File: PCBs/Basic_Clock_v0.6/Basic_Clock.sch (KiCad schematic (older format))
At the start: 37 parts, among them J1 Conn_01x04_Female, J3 Screw_Terminal_01x02, J4 Screw_Terminal_01x02, J5 Conn_01x03_Female, SW2 SW_Push, SW3 SW_Push, SW4 SW_Push, U1 LM317_TO-220, U2 ATmega328P-PU, U3 MAX485E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

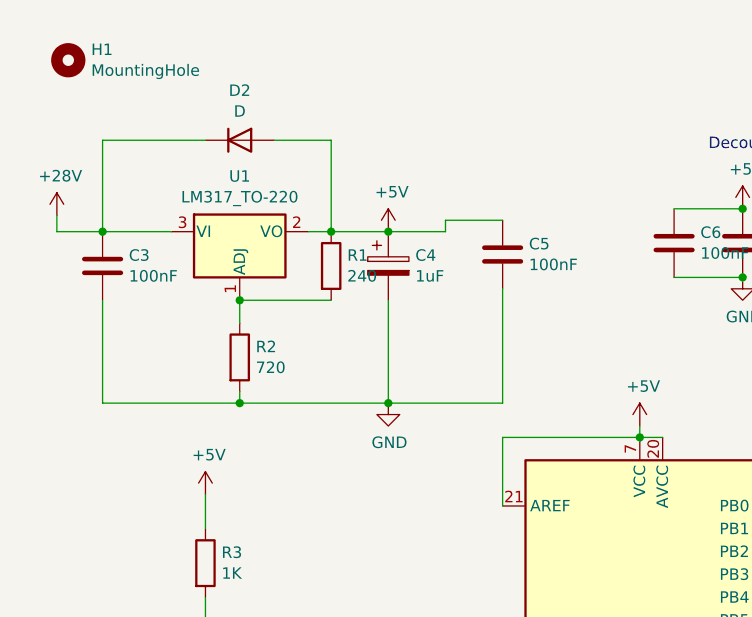
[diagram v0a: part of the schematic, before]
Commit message: Fixed ICSP Pinout
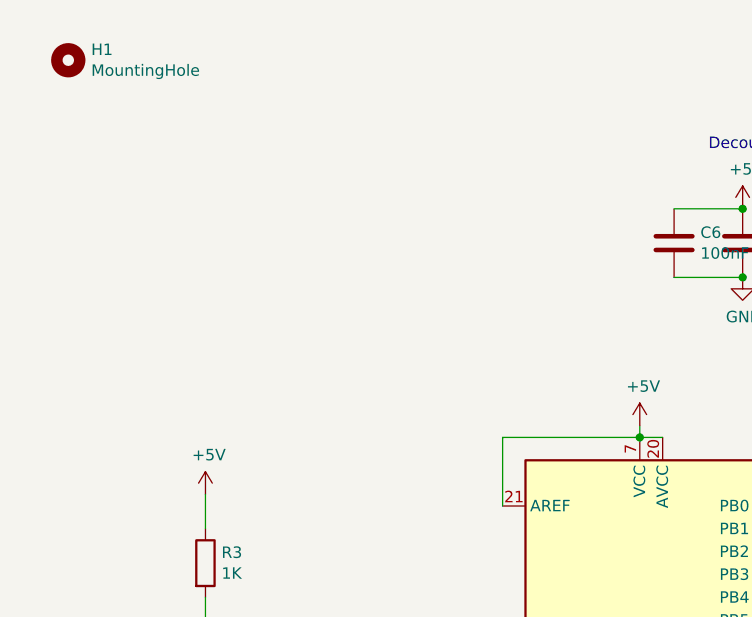
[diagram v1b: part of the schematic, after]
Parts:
- removed C3, C5: 100nF, Capacitor_THT:C_Rect_L7.0mm_W3.5mm_P5.00mm, symbol Device:C
- removed C4: 1uF, Capacitor THT:CP_Radial_D5.0mm_P2.00mm, symbol Device:CP
- removed D2: D, Diode THT:D_T-1_P10.16mm_Horizontal, symbol Device:D
- removed R1: 240, Resistor:R_Axial_DIN0309_L9.0mm_D3.2mm_P12.70mm_Horizontal, symbol Device:R
- removed R2: 720, Resistor:R_Axial_DIN0309_L9.0mm_D3.2mm_P12.70mm_Horizontal, symbol Device:R
- removed U1: LM317_TO-220, TO SOT THT:TO-220-3_Vertical, symbol Regulator_Linear:LM317_TO-220
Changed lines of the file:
@@
 	3350 5550 3350 5300
-$Comp
-L Regulator_Linear:LM317_TO-220 U1
-U 1 1 5F5E354F
-P 1600 1400
-F 0 "U1" H 1600 1642 50  0000 C CNN
-F 1 "LM317_TO-220" H 1600 1551 50  0000 C CNN
-F 2 "TO SOT THT:TO-220-3_Vertical" H 1600 1650 50  0001 C CIN
-F 3 "https://www.distrelec.ch/Web/Downloads/a_/en/tnSTM-LM317_data_en.pdf" H 1600 1400 50  0001 C CNN
-	1    1600 1400
-	1    0    0    -1
-$EndComp
 $Comp
 L Device:Crystal Y1
@@
 	1    0    0    -1
 $EndComp
-$Comp
-L Device:C C3
-U 1 1 5F5EFD99
-P 1000 1550
-F 0 "C3" H 1115 1596 50  0000 L CNN
-F 1 "100nF" H 1115 1505 50  0000 L CNN
-F 2 "Capacitor_THT:C_Rect_L7.0mm_W3.5mm_P5.00mm" H 1038 1400 50  0001 C CNN
-F 3 "https://www.distrelec.ch/en/ceramic-capacitor-100nf-50v-10-kemet-c322c104k5r5ta7301/p/16571681" H 1000 1550 50  0001 C CNN
-	1    1000 1550
-	1    0    0    -1
-$EndComp
-$Comp
-L Device:R R1
-U 1 1 5F5F0629
-P 2000 1550
-F 0 "R1" H 2070 1596 50  0000 L CNN
-F 1 "240" H 2070 1505 50  0000 L CNN
-F 2 "Resistor:R_Axial_DIN0309_L9.0mm_D3.2mm_P12.70mm_Horizontal" V 1930 1550 50  0001 C CNN
-F 3 "https://www.distrelec.ch/de/widerstand-600mw-240ohm-vishay-mbb02070c2400fct00/p/16059199?q=240ohm&pos=1&origPos=1&origPageSize=10&track=true" H 2000 1550 50  0001 C CNN
-	1    2000 1550
-	1    0    0    -1
-$EndComp
-$Comp
-L Device:R R2
-U 1 1 5F5F10C3
-P 1600 1950
-F 0 "R2" H 1670 1996 50  0000 L CNN
-F 1 "720" H 1670 1905 50  0000 L CNN
-F 2 "Resistor:R_Axial_DIN0309_L9.0mm_D3.2mm_P12.70mm_Horizontal" V 1530 1950 50  0001 C CNN
-F 3 "https://www.distrelec.ch/de/metallschicht-festwiderstand-fuer-durchsteckmontage-732ohm-600mw-rnd-components-rnd-155m207f732rtkrtb5k0/p/30155447?q=*&pos=1&origPos=974&origPageSize=10&track=true" H 1600 1950 50  0001 C CNN
-	1    1600 1950
-	1    0    0    -1
-$EndComp
-$Comp
-L Device:D D2
-U 1 1 5F5F1652
-P 1600 1000
-F 0 "D2" H 1600 1217 50  0000 C CNN
-F 1 "D" H 1600 1126 50  0000 C CNN
-F 2 "Diode THT:D_T-1_P10.16mm_Horizontal" H 1600 1000 50  0001 C CNN
-F 3 "https://www.distrelec.ch/Web/Downloads/_t/ds/1n400x_eng_tds.pdf" H 1600 1000 50  0001 C CNN
-	1    1600 1000
-	1    0    0    -1
-$EndComp
-$Comp
-L Device:CP C4
-U 1 1 5F5F1EDA
-P 2250 1550
-F 0 "C4" H 2368 1596 50  0000 L CNN
-F 1 "1uF" H 2368 1505 50  0000 L CNN
-F 2 "Capacitor THT:CP_Radial_D5.0mm_P2.00mm" H 2288 1400 50  0001 C CNN
-F 3 "https://www.distrelec.ch/en/radial-electrolytic-capacitor-1uf-25vdc-20-rnd-components-rnd-150ehr010m25b/p/30091992?q=1uF&pos=3&origPos=3&origPageSize=10&track=true" H 2250 1550 50  0001 C CNN
-	1    2250 1550
-	1    0    0    -1
-$EndComp
-Wire Wire Line
-	1000 1400 1300 1400
-Wire Wire Line
-	1900 1400 2000 1400
-Wire Wire Line
-	2000 1400 2250 1400
-Connection ~ 2000 1400
-Wire Wire Line
-	2000 1700 1600 1700
-Wire Wire Line
-	1000 2150 1000 1700
-Wire Wire Line
-	2000 1400 2000 1000
-Wire Wire Line
-	2000 1000 1750 1000
-Wire Wire Line
-	1450 1000 1000 1000
-Wire Wire Line
-	1000 1000 1000 1400
-Connection ~ 1000 1400
-$Comp
-L power:+28V #PWR0107
-U 1 1 5F5F7051
-P 800 1330
-F 0 "#PWR0107" H 800 1180 50  0001 C CNN
-F 1 "+28V" H 815 1503 50  0000 C CNN
-F 2 "" H 1050 1380 50  0001 C CNN
-F 3 "" H 1050 1380 50  0001 C CNN
-	1    800  1330
-	1    0    0    -1
-$EndComp
-Wire Wire Line
-	1000 1400 800  1400
-$Comp
-L power:+5V #PWR0109
-U 1 1 5F5FB9F2
-P 2250 1400
-F 0 "#PWR0109" H 2250 1250 50  0001 C CNN
-F 1 "+5V" H 2265 1573 50  0000 C CNN
-F 2 "" H 2250 1400 50  0001 C CNN
-F 3 "" H 2250 1400 50  0001 C CNN
-	1    2250 1400
-	1    0    0    -1
-$EndComp
-Connection ~ 2250 1400
-Wire Wire Line
-	1000 2150 1600 2150
-Wire Wire Line
-	1600 1800 1600 1700
-Connection ~ 1600 1700
-Wire Wire Line
-	1600 2100 1600 2150
 $Comp
 L Device:LED D1
@@
 Wire Wire Line
 	4950 4100 3950 4100
-$Comp
-L power:GND #PWR0108
-U 1 1 5F5F7878
-P 2250 2150
-F 0 "#PWR0108" H 2250 1900 50  0001 C CNN
-F 1 "GND" H 2255 1977 50  0000 C CNN
-F 2 "" H 2250 2150 50  0001 C CNN
-F 3 "" H 2250 2150 50  0001 C CNN
-	1    2250 2150
-	1    0    0    -1
-$EndComp
-Wire Wire Line
-	1600 2150 2250 2150
-Connection ~ 1600 2150
-Wire Wire Line
-	2250 2150 2250 1700
-Connection ~ 2250 2150
-Wire Wire Line
-	2250 2150 2750 2150
-Wire Wire Line
-	2750 2150 2750 1650
-$Comp
-L Device:C C5
-U 1 1 5F627055
-P 2750 1500
-F 0 "C5" H 2865 1546 50  0000 L CNN
-F 1 "100nF" H 2865 1455 50  0000 L CNN
-F 2 "Capacitor_THT:C_Rect_L7.0mm_W3.5mm_P5.00mm" H 2788 1350 50  0001 C CNN
-F 3 "https://www.distrelec.ch/en/ceramic-capacitor-100nf-50v-10-kemet-c322c104k5r5ta7301/p/16571681" H 2750 1500 50  0001 C CNN
-	1    2750 1500
-	1    0    0    -1
-$EndComp
-Wire Wire Line
-	2750 1350 2500 1350
-Wire Wire Line
-	2500 1350 2500 1400
-Wire Wire Line
-	2500 1400 2250 1400
 Connection ~ 3950 2600
 Connection ~ 3950 2700
@@
 Wire Wire Line
 	3950 2600 4100 2600
-Wire Wire Line
-	800  1330 800  1400
 $Comp
 L power:+28V #PWR0119
